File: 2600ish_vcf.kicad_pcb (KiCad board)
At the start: 2 copper layers, 50 x 99.8 mm, 98 parts, among them J1 AUDIO IN 1, J2 AUDIO IN 2, J3 OUT, J4 V/OCT IN, J5 CV 1, J6 CV2, P1 50K log, P2 50K log, P3 50K lin, P4 100k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

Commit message: component placement done
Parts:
- removed J6: CV2, Connector_Audio:Jack_3.5mm_QingPu_WQP-PJ398SM_Vertical_CircularHoles
- removed P6: 50K lin, Potentiometer_THT:Potentiometer_Alpha_RD901F-40-00D_Single_Vertical
- removed R30: 100k, Resistor_THT:R_Axial_DIN0207_L6.3mm_D2.5mm_P7.62mm_Horizontal
- moved R8 308.0 mm to (199.9, 75.1), turned to 180 degrees
- moved Q3 294.6 mm to (202.2, 58.5), turned to -90 degrees
- moved Q4 290.4 mm to (202.3, 65.6), turned to -90 degrees
- moved R29 289.9 mm to (199.1, 58.8), turned to 180 degrees
- moved Q1 287.2 mm to (186.3, 63.8), turned to 90 degrees
- moved Q2 287.2 mm to (186.3, 71.1), turned to 90 degrees
- moved R45 270.6 mm to (180.6, 59.3), turned to 180 degrees
- moved R25 247.6 mm to (182.6, 86.1), turned to 180 degrees
- moved R27 241.2 mm to (176.4, 92.2)
- moved R24 237.1 mm to (175.0, 89.2)
- moved R23 236.1 mm to (175.0, 83.0)
- moved R26 234.9 mm to (171.0, 84.9), turned to -90 degrees
- moved Q11 233.7 mm to (181.4, 94.8), turned to -90 degrees
- moved Q12 225.5 mm to (175.8, 94.8), turned to -90 degrees
- moved C6 220.7 mm to (170.9, 99.8), turned to 90 degrees
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
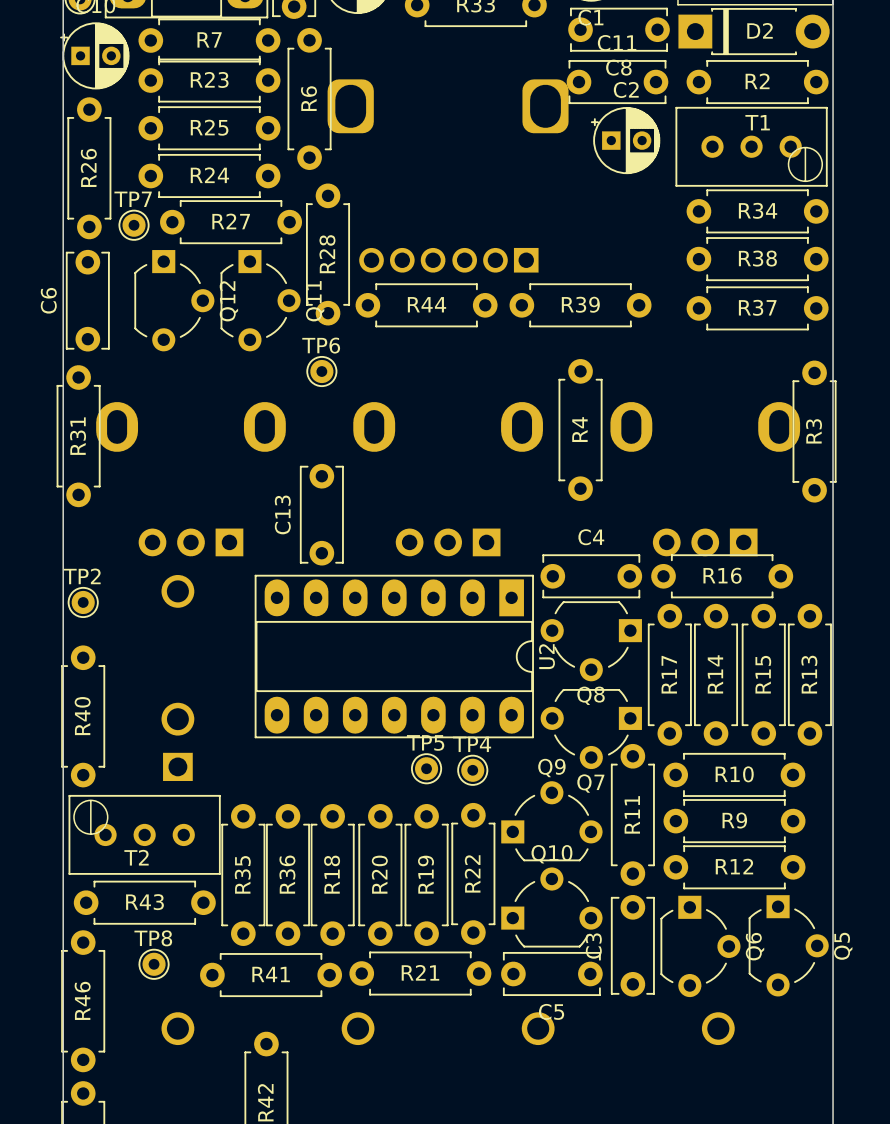
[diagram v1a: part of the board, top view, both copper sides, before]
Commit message: Some adjustments made for gain and footprint size
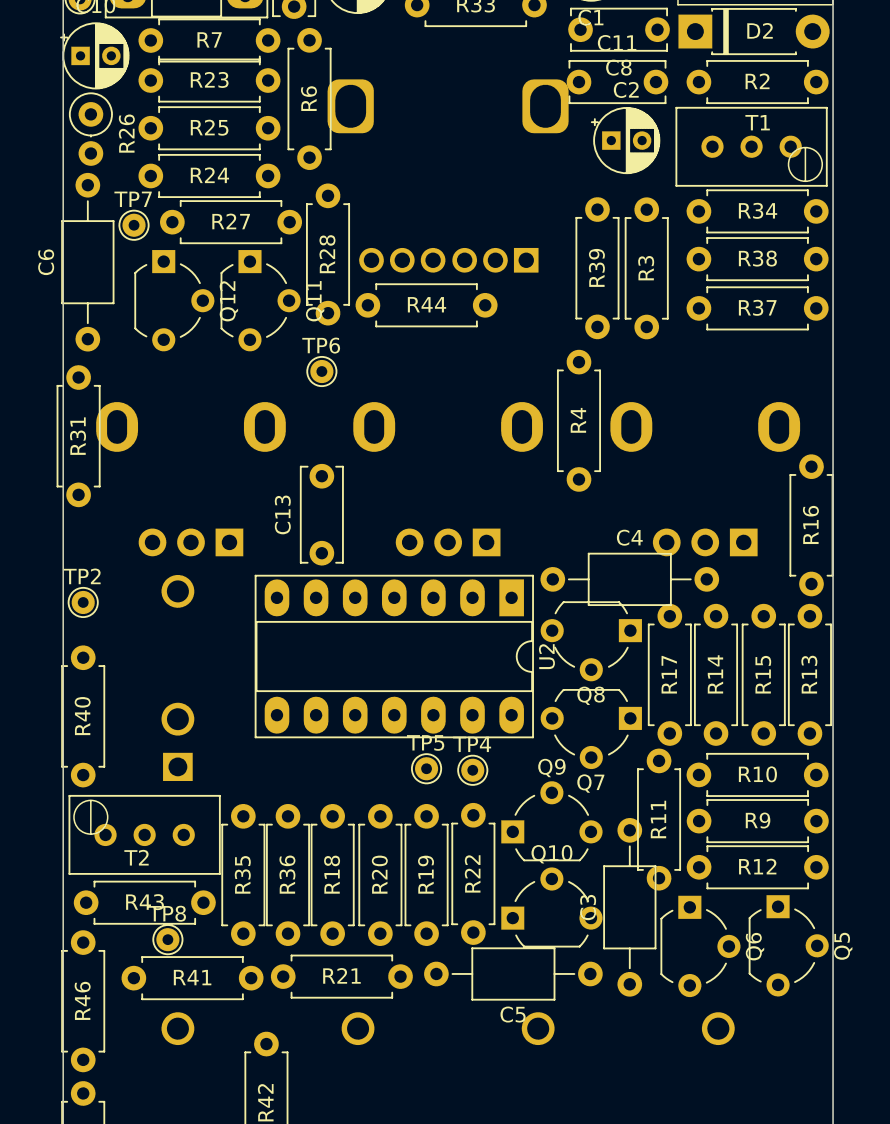
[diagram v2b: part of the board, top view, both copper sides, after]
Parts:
- C3, C4, C5, C6: footprint Capacitor_THT:C_Disc_D6.0mm_W2.5mm_P5.00mm -> Capacitor_THT:C_Axial_L5.1mm_D3.1mm_P10.00mm_Horizontal
- R26: footprint Resistor_THT:R_Axial_DIN0207_L6.3mm_D2.5mm_P7.62mm_Horizontal -> Resistor_THT:R_Axial_DIN0207_L6.3mm_D2.5mm_P2.54mm_Vertical
- R41: value 56k -> 100k
- moved R3 15.2 mm to (207.2, 99.0)
- moved R39 5.11 mm to (204.0, 99.0), turned to 90 degrees
- moved R41 5.10 mm to (173.9, 141.3)
- moved R21 5.10 mm to (183.6, 141.2)
- moved R16 2.05 mm to (217.9, 115.7), turned to 90 degrees
- moved TP8 1.84 mm to (176.1, 138.8)
- moved R11 1.73 mm to (208.0, 127.2)
- moved R10 1.51 mm to (210.6, 128.1)
- moved R12 1.51 mm to (210.6, 134.1)
- moved R9 1.51 mm to (210.6, 131.1)
- moved R4 0.61 mm to (202.8, 108.9)
- moved R26 0.33 mm to (171.1, 85.2)
- moved C4 0.20 mm to (201.1, 115.4)
- moved C3 0.20 mm to (206.1, 141.7)

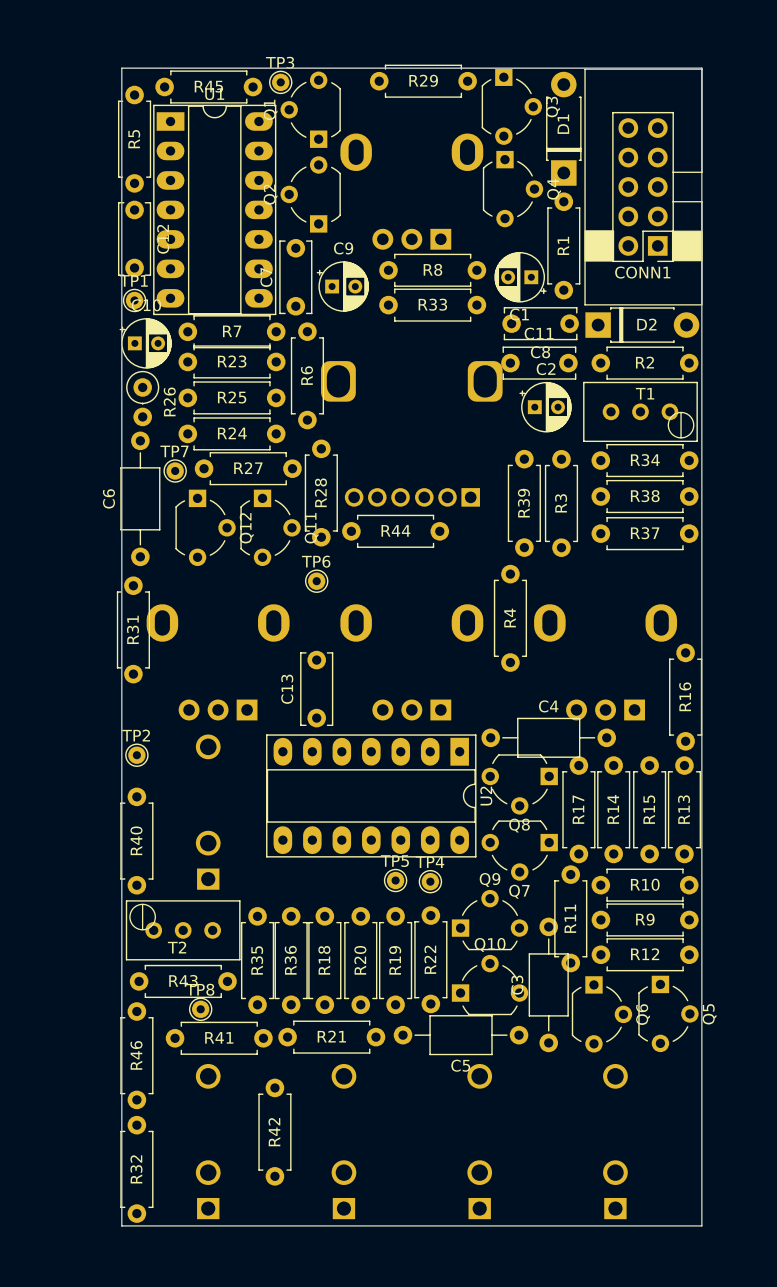
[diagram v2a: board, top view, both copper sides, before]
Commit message: Clearer schematic
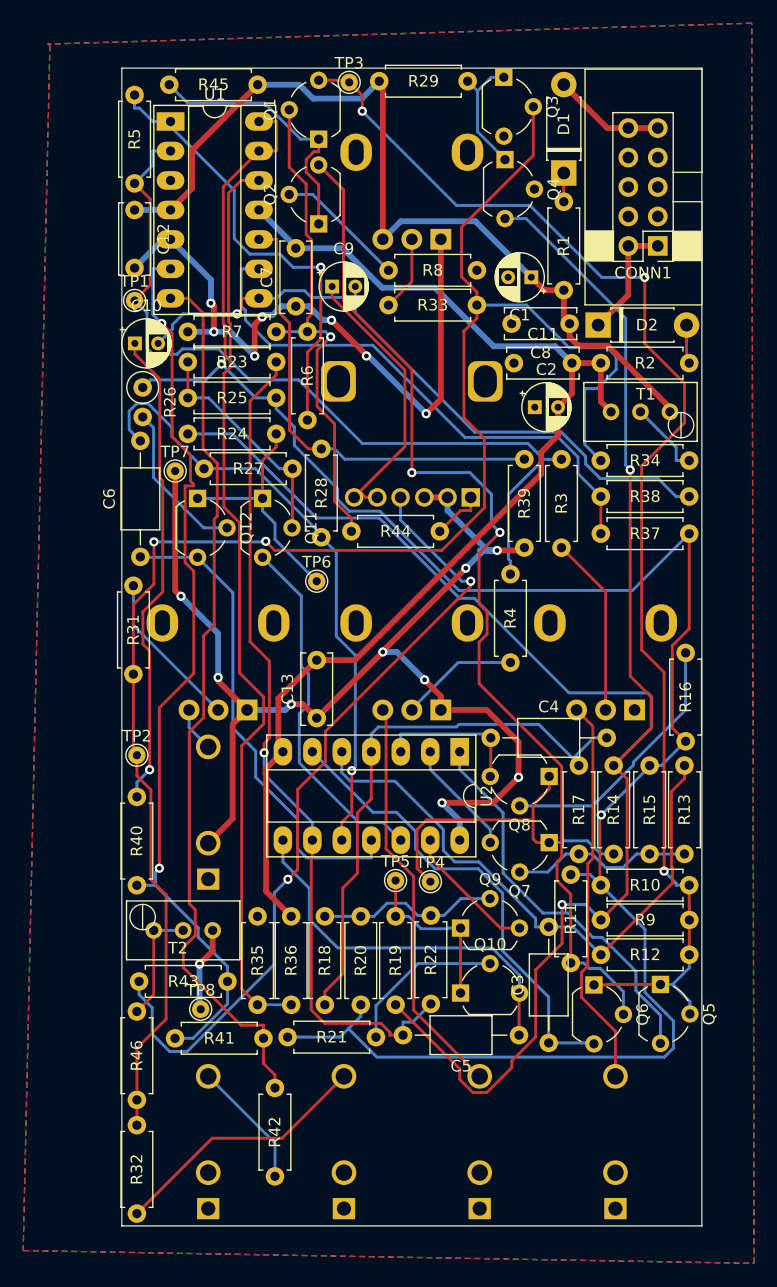
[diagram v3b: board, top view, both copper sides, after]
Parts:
- moved R45 7.22 mm to (173.4, 59.1), turned to 0 degrees
- moved TP3 5.90 mm to (188.9, 58.9)
- moved C11 0.30 mm to (203.1, 83.1)
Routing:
- net Net-(U1D--): track 0.00 -> 177.6 mm, vias 0 -> 2
- net GND: track 0.00 -> 172.4 mm, vias 0 -> 17
- net Net-(Q4-C): track 0.00 -> 160.5 mm, vias 0 -> 2
- net CUTOFF: track 0.00 -> 147.6 mm, vias 0 -> 2
- net Net-(Q1-C): track 0.00 -> 112.8 mm, vias 0 -> 3
- net -12V: track 0.00 -> 101.3 mm
- net Net-(Q2-C): track 0.00 -> 90.6 mm, vias 0 -> 2
- net Net-(U1D-+): track 0.00 -> 79.0 mm
- net Net-(U1B--): track 0.00 -> 78.7 mm, vias 0 -> 2
- net +12V: track 0.00 -> 76.8 mm
- net Net-(R41-Pad2): track 0.00 -> 76.7 mm
- net Net-(C5-Pad2): track 0.00 -> 72.5 mm, vias 0 -> 1
- net Net-(U1A--): track 0.00 -> 72.0 mm
- net Net-(P4-Pad5): track 0.00 -> 69.5 mm, vias 0 -> 2
- net Net-(C10-Pad2): track 0.00 -> 57.9 mm, vias 0 -> 1
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- added copper zone on B.Cu, net GND
- added copper zone on F.Cu, net GND

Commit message: Schematic for split board done, updating PCB now
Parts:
- added J6: Conn_01x08_Pin, Connector_PinHeader_2.54mm:PinHeader_2x04_P2.54mm_Vertical, F.Cu at (143.5, 92.3)
- added J7: Conn_01x08_Socket, Connector_PinSocket_2.54mm:PinSocket_2x04_P2.54mm_Vertical, F.Cu at (138.8, 92.3)
- added J8: Conn_01x04_Pin, Connector_PinHeader_2.54mm:PinHeader_1x04_P2.54mm_Vertical, F.Cu at (127.1, 92.3)
- added J9: Conn_01x04_Socket, Connector_PinSocket_2.54mm:PinSocket_1x04_P2.54mm_Vertical, F.Cu at (131.7, 92.3)
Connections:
- net Net-(C9-Pad1) renamed RESONANCE 3
- net Net-(P4-Pad5) renamed RESONANCE 2
- net Net-(Q1-B) renamed RESONANCE 1
- net Net-(R41-Pad2) renamed AUDIO OUT
- net Net-(U1A--) renamed AUDIOS IN

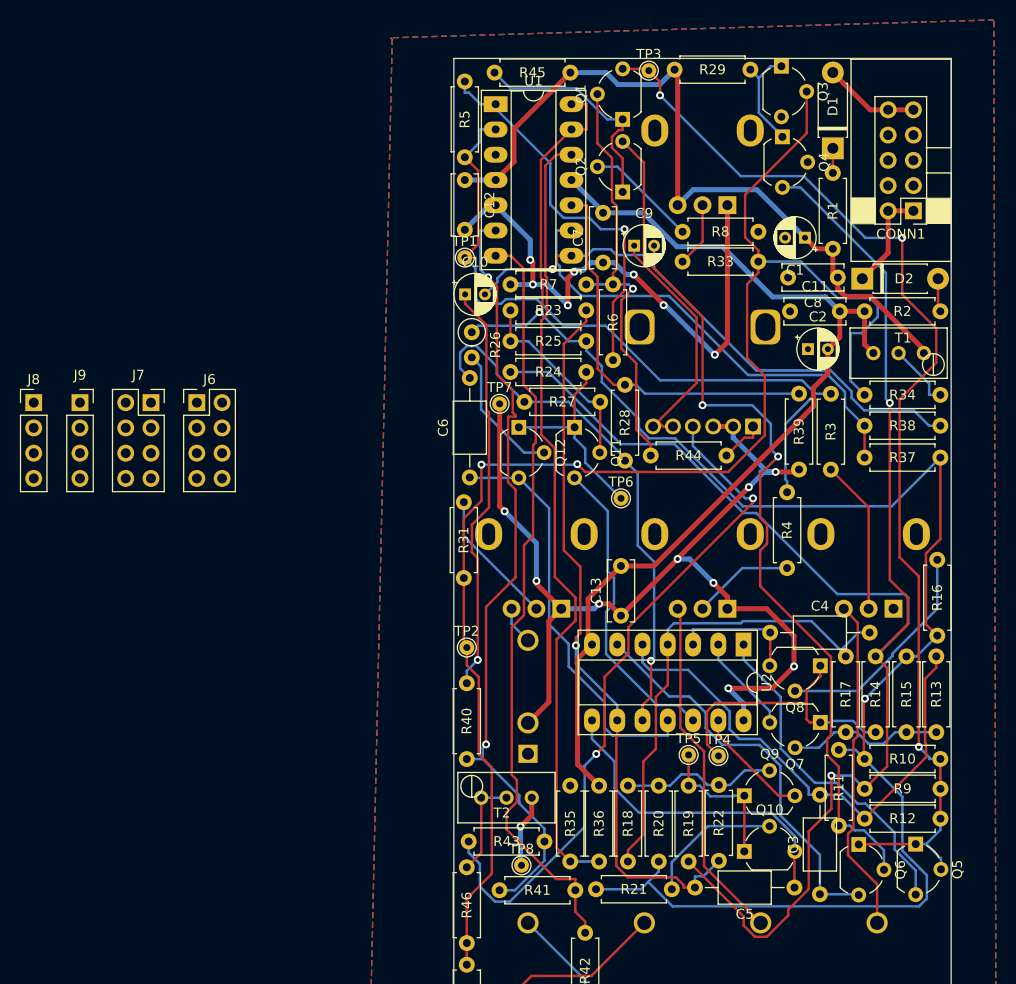
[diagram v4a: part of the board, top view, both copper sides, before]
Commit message: Main PCB pretty much done, panel work started
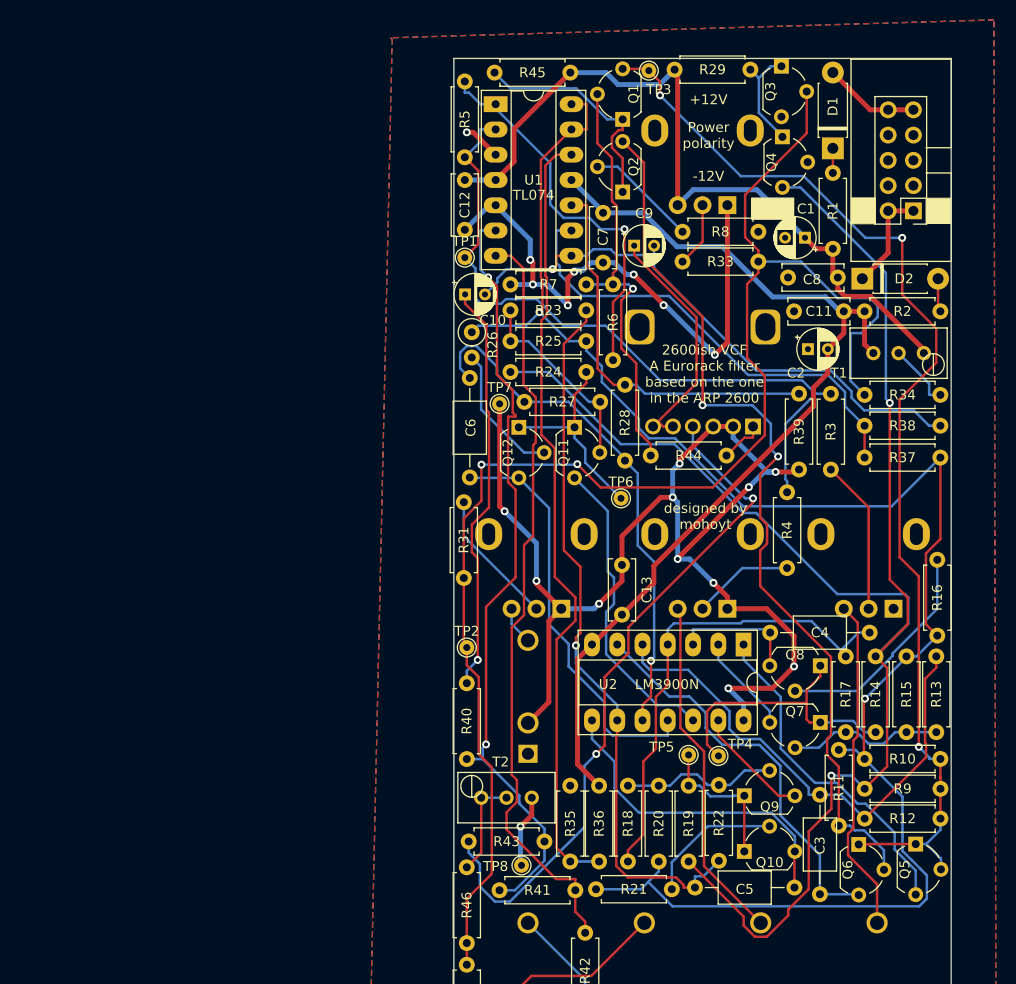
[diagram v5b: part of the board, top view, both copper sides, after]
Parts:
- removed J6: Conn_01x08_Pin, Connector_PinHeader_2.54mm:PinHeader_2x04_P2.54mm_Vertical
- removed J7: Conn_01x08_Socket, Connector_PinSocket_2.54mm:PinSocket_2x04_P2.54mm_Vertical
- removed J8: Conn_01x04_Pin, Connector_PinHeader_2.54mm:PinHeader_1x04_P2.54mm_Vertical
- removed J9: Conn_01x04_Socket, Connector_PinSocket_2.54mm:PinSocket_1x04_P2.54mm_Vertical
- moved C13 5.10 mm to (186.2, 108.6), turned to -90 degrees
- moved C11 0.40 mm to (203.5, 83.1)
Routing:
- net GND: track 172.4 -> 192.5 mm, vias 17 -> 20
- net -12V: track 101.3 -> 98.7 mm
- net CUTOFF: track 147.6 -> 148.4 mm
- net +12V: track 76.8 -> 76.0 mm
- net Net-(Q8-C): track 12.8 -> 12.2 mm
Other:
- board text added: "+12V"
- board text added: "-12V"
- board text added: "2600ish VCF A Eurorack filter based on the one in the ARP 2600"
- board text added: "AUDIO 1"
- board text added: "AUDIO 2"
- board text added: "AUDIO IN 1"
- board text added: "AUDIO IN 2"
- board text added: "AUDIO OUT"
- board text added: "CUTOFF"
- board text added: "CV1"
- board text added: "LM3900N"
- board text added: "Power polarity"
- board text added: "RESONANCE"
- board text added: "TL074"
- board text added: "V/OCT IN"
- board text added: "designed by mohoyt"

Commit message: New panel design with topography
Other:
- board text added: "V/Oct trimmer"
- board text added: "WayWayWay"
- board text added: "low freq trimmer"
- board text added: "transistors are 2N3906 matched pairs C3 to C6 should be polystyrene or silver-mica 470pF caps"
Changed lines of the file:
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@@
       (disableapertmacros false)
       (usegerberextensions false)
-      (usegerberattributes true)
-      (usegerberadvancedattributes true)
-      (creategerberjobfile true)
+      (usegerberattributes false)
+      (usegerberadvancedattributes false)
+      (creategerberjobfile false)
       (dashed_line_dash_ratio 12.000000)
       (dashed_line_gap_ratio 3.000000)
@@
       (psa4output false)
       (plotreference true)
-      (plotvalue true)
+      (plotvalue false)
       (plotinvisibletext false)
       (sketchpadsonfab false)
-      (subtractmaskfromsilk false)
+      (subtractmaskfromsilk true)
       (outputformat 1)
       (mirror false)
-      (drillshape 1)
+      (drillshape 0)
       (scaleselection 1)
-      (outputdirectory "")
+      (outputdirectory "gerbers/")
     )
   )
@@
     )
   )
+  (gr_line (start 180.46 122.5) (end 179.475 129.46)
+    (stroke (width 0.15) (type default)) (layer "F.SilkS"))
+  (gr_line (start 209.125 89.84) (end 208.84 102.19)
+    (stroke (width 0.15) (type default)) (layer "F.SilkS"))
   (gr_rect (start 199.25 71.726) (end 203.45 73.826)
     (stroke (width 0.15) (type solid)) (fill solid) (layer "F.SilkS"))
@@
     (effects (font (size 1 1) (thickness 0.15)) (justify left bottom mirror))
   )
+  (gr_text "WayWayWay" (at 181.71 108.76) (layer "B.SilkS")
+    (effects (font (size 1 1) (thickness 0.15)) (justify left bottom mirror))
+  )
   (gr_text "designed by \nmohoyt" (at 194.6 105.1) (layer "F.SilkS")
     (effects (font (size 1 1) (thickness 0.15)) (justify bottom))
@@
     (effects (font (size 1 1) (thickness 0.15)) (justify bottom))
   )
+  (gr_text "transistors are 2N3906 matched pairs\nC3 to C6 should be polystyrene \nor silver-mica 470pF caps" (at 186.58 150.69) (layer "F.SilkS")
+    (effects (font (size 1 1) (thickness 0.15)) (justify left bottom))
+  )
   (gr_text "2600ish VCF\nA Eurorack filter \nbased on the one \nin the ARP 2600" (at 194.5 92.4) (layer "F.SilkS")
     (effects (font (size 1 1) (thickness 0.15)) (justify bottom))
   )
+  (gr_text "low freq\ntrimmer" (at 212.24 104.07) (layer "F.SilkS")
+    (effects (font (size 1 1) (thickness 0.15)) (justify bottom))
+  )
+  (gr_text "V/Oct\ntrimmer" (at 178.47 122.18) (layer "F.SilkS")
+    (effects (font (size 1 1) (thickness 0.15)) (justify bottom))
+  )
